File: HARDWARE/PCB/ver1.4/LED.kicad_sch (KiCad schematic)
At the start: 52 parts

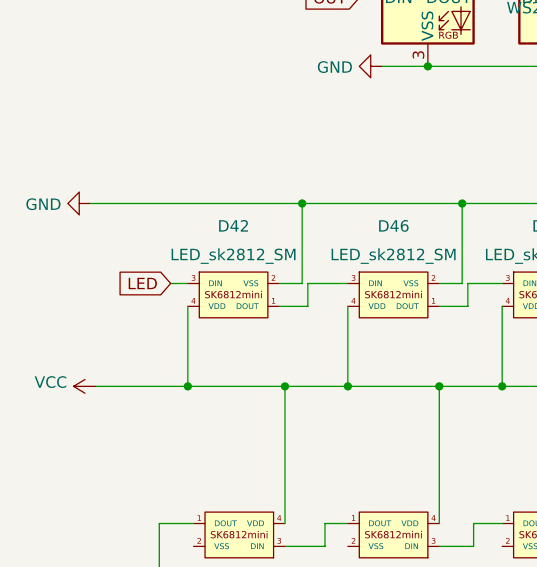
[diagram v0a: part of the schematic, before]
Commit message: FEAT: add selector for underglow or matrix
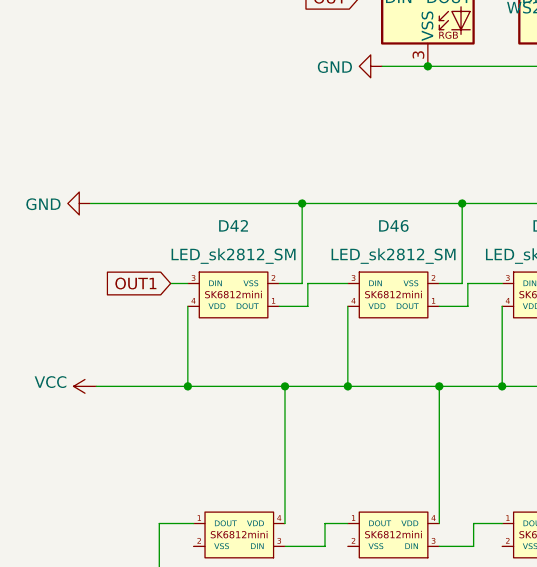
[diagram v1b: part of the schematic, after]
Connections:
- net LED renamed OUT1
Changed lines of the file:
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@@
     (stroke (width 0) (type default))
   )
-  (global_label "LED" (shape input) (at 53.34 67.31 180) (fields_autoplaced)
+  (global_label "OUT1" (shape input) (at 53.34 67.31 180) (fields_autoplaced)
     (effects (font (size 1.27 1.27)) (justify right))
-    (property "Intersheetrefs" "${INTERSHEET_REFS}" (at 47.6413 67.31 0)
+    (property "Intersheetrefs" "${INTERSHEET_REFS}" (at 46.2503 67.31 0)
       (effects (font (size 1.27 1.27)) (justify right) hide)
     )
